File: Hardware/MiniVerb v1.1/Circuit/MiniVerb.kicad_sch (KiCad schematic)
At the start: 40 parts, among them U1 TL074, U2 TL074

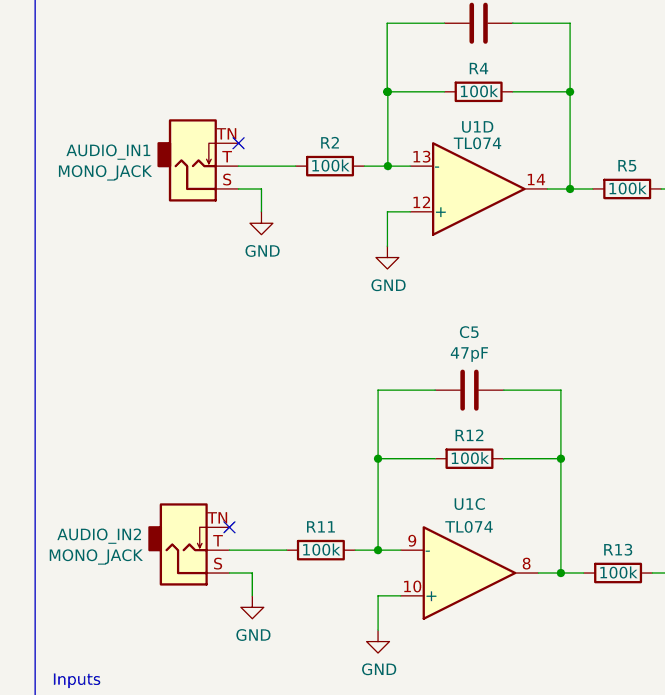
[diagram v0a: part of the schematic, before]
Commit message: Use TN pin for IN (R)
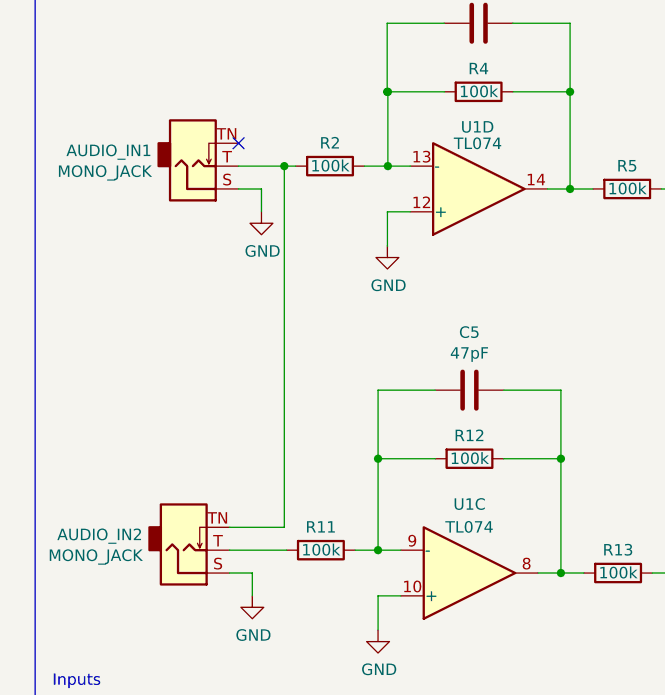
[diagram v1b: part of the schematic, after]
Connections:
- net at AUDIO_IN1.T, R2.2: now also AUDIO_IN2.TN
- no-connect marks 25 -> 24
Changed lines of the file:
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@@
   (junction (at 87.884 84.074) (diameter 0) (color 0 0 0 0)
+  )
+  (junction (at 43.18 38.862) (diameter 0) (color 0 0 0 0)
   )
   (junction (at 47.625 174.752) (diameter 0) (color 0 0 0 0)
@@
   (no_connect (at 261.366 92.964))
   (no_connect (at 261.366 90.424))
-  (no_connect (at 37.084 78.994))
   (no_connect (at 118.11 131.572))
   (no_connect (at 117.475 177.292))
@@
     (stroke (width 0) (type default) (color 0 0 0 0))
   )
+  (wire (pts (xy 43.18 78.994) (xy 43.18 38.862))
+    (stroke (width 0) (type default) (color 0 0 0 0))
+  )
   (wire (pts (xy 83.82 136.652) (xy 83.82 140.462))
     (stroke (width 0) (type default) (color 0 0 0 0))
@@
     (stroke (width 0) (type default) (color 0 0 0 0))
   )
+  (wire (pts (xy 43.18 38.862) (xy 44.45 38.862))
+    (stroke (width 0) (type default) (color 0 0 0 0))
+  )
   (wire (pts (xy 165.862 101.092) (xy 165.862 103.124))
     (stroke (width 0) (type default) (color 0 0 0 0))
@@
     (stroke (width 0) (type default) (color 0 0 0 0))
   )
-  (wire (pts (xy 38.1 38.862) (xy 44.45 38.862))
+  (wire (pts (xy 38.1 38.862) (xy 43.18 38.862))
     (stroke (width 0) (type default) (color 0 0 0 0))
   )
@@
     (stroke (width 0) (type default) (color 0 0 0 0))
   )
+  (wire (pts (xy 37.084 78.994) (xy 43.18 78.994))
+    (stroke (width 0) (type default) (color 0 0 0 0))
+  )

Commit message: Updated BOM
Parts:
- AUDIO_IN1, AUDIO_IN2, AUDIO_OUT1, AUDIO_OUT2: Manufacturers Name (none) -> Tayda Electronics; Manufacturers Part Number (none) -> PJ-3001F
- C1, C2, C4, C5, C7, C8: Manufacturers Name (none) -> Murata Electronics; Manufacturers Part Number (none) -> RDE5C2A470J0M1H03A
- C3, C6: value 580pF -> 680pF; Manufacturers Name (none) -> Murata Electronics; Manufacturers Part Number (none) -> RCE7U2J681J2M1H03A; Part Description (none) -> Replaced 580pF from original circuit
- POT_DRY1, POT_FBK1, POT_LPF1, POT_MOD1, POT_WET1: Manufacturers Name (none) -> Alpha (Taiwan); Manufacturers Part Number (none) -> RD901F-40-15R1-B10K
- R1, R14, R16, R7: Manufacturers Name (none) -> KOA Speer; Manufacturers Part Number (none) -> MF1/4DC1002F
- R10, R15, R20, R9: Manufacturers Name (none) -> KOA Speer; Manufacturers Part Number (none) -> MF1/4DCT26A1001F
- R11, R12, R13, R17, R18, R19, R2, R3, R4, R5, R6, R8: Manufacturers Name (none) -> Vishay / Dale; Manufacturers Part Number (none) -> CCF55100KFKE36
- U1, U2: Manufacturers Name (none) -> Texas Instruments; Manufacturers Part Number (none) -> TL074BCN
